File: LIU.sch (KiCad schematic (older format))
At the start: 96 parts, among them J1 Audio Input, J2 Audio Input, J3 12 Volts Input, J4 Audio Output, J5 Audio Output, U1 PT2399, U2 PT2399, U3 L7805, U4 M5226P, U5 M5226P

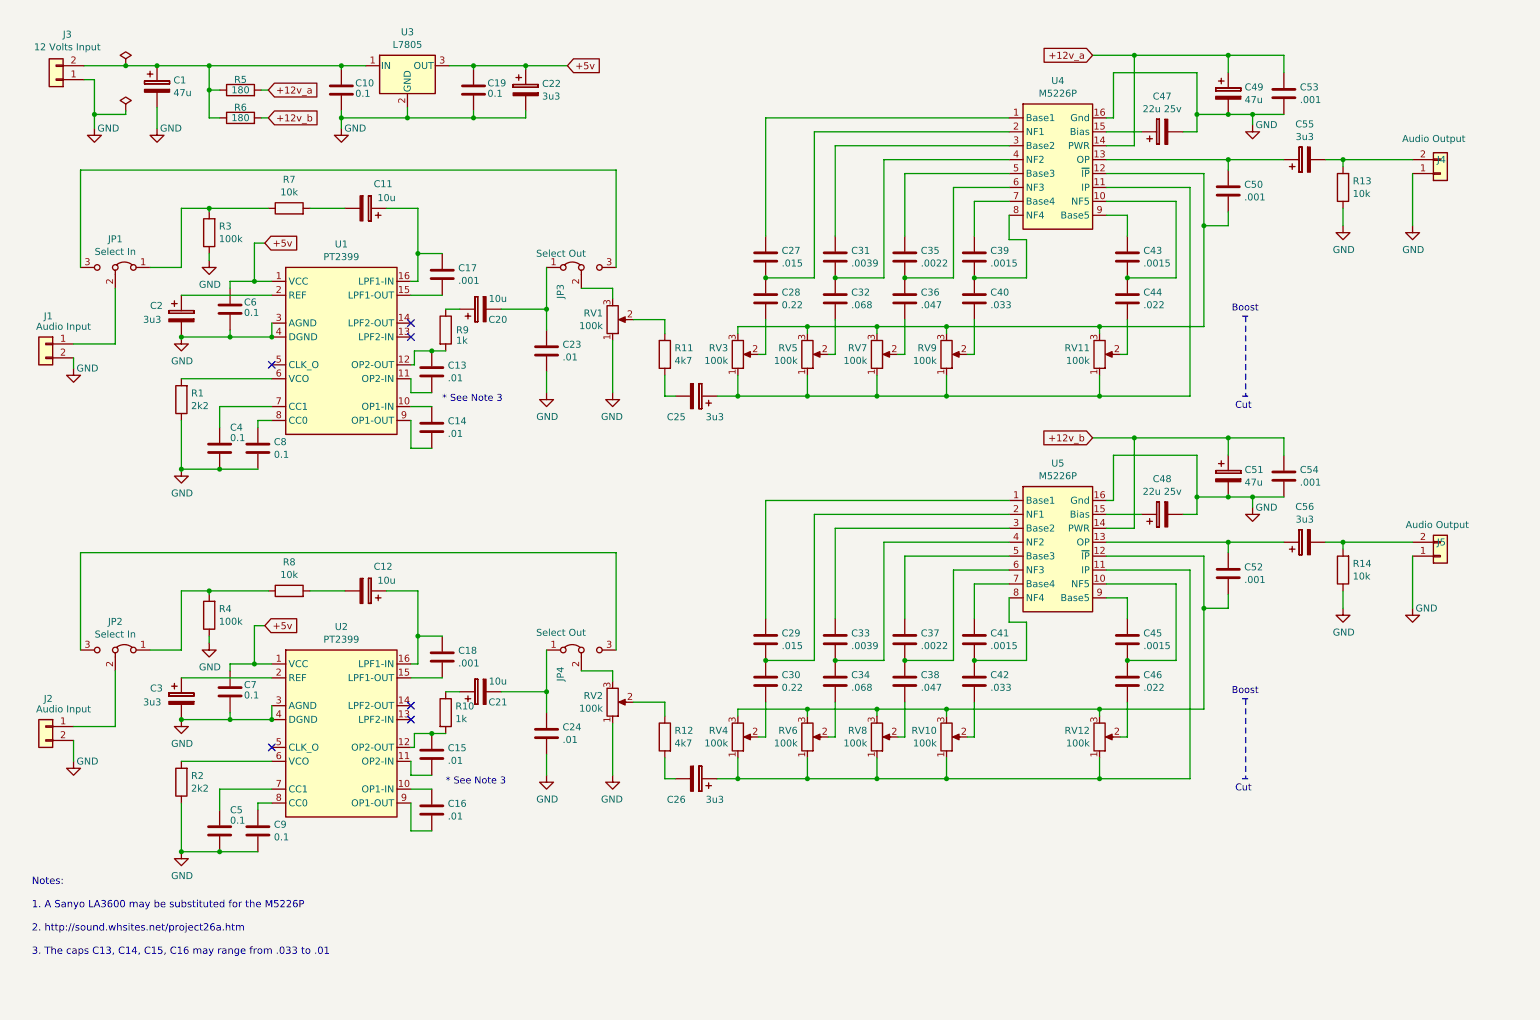
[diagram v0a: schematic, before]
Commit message: Created space in schematic for signaling wiring
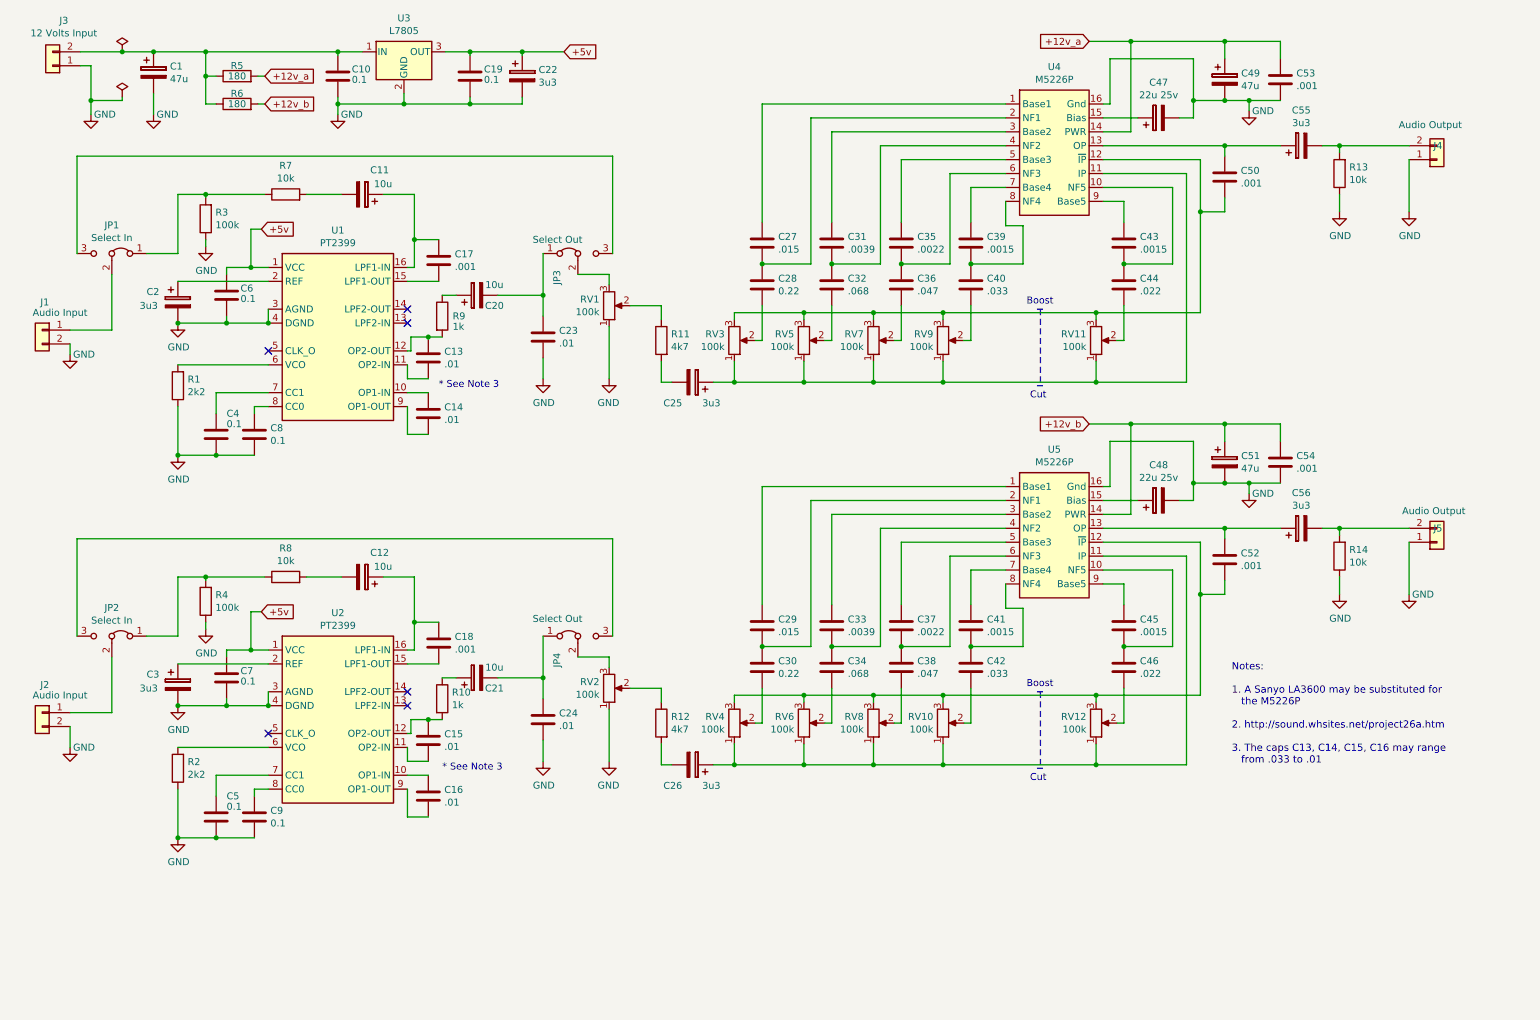
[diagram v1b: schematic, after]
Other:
- note added: "Notes:\n\n1. A Sanyo LA3600 may be substituted for\n the M5226P\n\n2. http://sound.whsites.net/project26a.htm\n\n3. The caps C13, C14, C15, C16 may range\n from .033 to .01\n"
- note removed: "Notes:\n\n1. A Sanyo LA3600 may be substituted for the M5226P\n\n2. http://sound.whsites.net/project26a.htm\n\n3. The caps C13, C14, C15, C16 may range from .033 to .01\n"
- moved on the sheet: C1, C10, C11, C12, C13, C14, C15, C16, C17, C18, C19, C2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

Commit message: Schematic finalised & layout commenced
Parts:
- removed R2: 2k2, symbol Device:R
- added D1, D2: LED_ALT, LED_SMD:LED_1206_3216Metric_Pad1.42x1.75mm_HandSolder, symbol Device:LED_ALT
- added H1, H2, H3, H4: MountingHole, MountingHole:MountingHole_3.2mm_M3, symbol Mechanical:MountingHole
- added J3: UHF out, Connector_PinHeader_2.54mm:PinHeader_1x02_P2.54mm_Vertical, symbol Connector_Generic:Conn_01x02
- added J4: UHF in, Connector_PinHeader_2.54mm:PinHeader_1x02_P2.54mm_Vertical, symbol Connector_Generic:Conn_01x02
- added J6: VHF in, Connector_PinHeader_2.54mm:PinHeader_1x02_P2.54mm_Vertical, symbol Connector_Generic:Conn_01x02
- added J7: VHF out, Connector_PinHeader_2.54mm:PinHeader_1x02_P2.54mm_Vertical, symbol Connector_Generic:Conn_01x02
- added Q1, Q2: 2N7002, Package_TO_SOT_SMD:SOT-23_Handsoldering, symbol Transistor_FET:2N7002
- added R10, R9: 100k, Resistor_SMD:R_1206_3216Metric_Pad1.42x1.75mm_HandSolder, symbol Device:R
- added R13, R14: 10k, Resistor_SMD:R_1206_3216Metric_Pad1.42x1.75mm_HandSolder, symbol Device:R
- added R15, R18, R4: 2k2, Resistor_SMD:R_1206_3216Metric_Pad1.42x1.75mm_HandSolder, symbol Device:R
- added RV1, RV2: 10k, Potentiometer_THT:Potentiometer_Bourns_3386P_Vertical, symbol Device:R_POT
- C1, C49, C51: footprint (none) -> Capacitor_SMD:CP_Elec_6.3x5.2
- C10, C13, C14, C15, C16, C17, C18, C19, C23, C24, C27, C28, C29, C30, C31, C32, C33, C34, C35, C36, C37, C38, C39, C4, C40, C41, C42, C43, C44, C45, C46, C5, C50, C52, C53, C54, C6, C7, C8, C9: footprint (none) -> Capacitor_SMD:C_1206_3216Metric_Pad1.42x1.75mm_HandSolder
- C11, C12, C2, C20, C21, C22, C25, C26, C3, C47, C48, C55, C56: footprint (none) -> Capacitor_SMD:CP_Elec_5x5.3
- J1, J2: footprint (none) -> Connector_PinHeader_2.54mm:PinHeader_1x02_P2.54mm_Vertical
- J5: renamed from J3; footprint (none) -> Connector_PinHeader_2.54mm:PinHeader_1x02_P2.54mm_Vertical
- J8: renamed from J4; footprint (none) -> Connector_PinHeader_2.54mm:PinHeader_1x02_P2.54mm_Vertical
- J9: renamed from J5; footprint (none) -> Connector_PinHeader_2.54mm:PinHeader_1x02_P2.54mm_Vertical
- JP1, JP2, JP3, JP4: footprint (none) -> Connector_PinHeader_2.54mm:PinHeader_1x03_P2.54mm_Vertical
- R1: renamed from R3; footprint (none) -> Resistor_SMD:R_1206_3216Metric_Pad1.42x1.75mm_HandSolder
- R11: renamed from R9; footprint (none) -> Resistor_SMD:R_1206_3216Metric_Pad1.42x1.75mm_HandSolder
- R12: renamed from R10; footprint (none) -> Resistor_SMD:R_1206_3216Metric_Pad1.42x1.75mm_HandSolder
- R16: renamed from R11; footprint (none) -> Resistor_SMD:R_1206_3216Metric_Pad1.42x1.75mm_HandSolder
- R17: renamed from R12; footprint (none) -> Resistor_SMD:R_1206_3216Metric_Pad1.42x1.75mm_HandSolder
- R19: renamed from R13; footprint (none) -> Resistor_SMD:R_1206_3216Metric_Pad1.42x1.75mm_HandSolder
- R2: renamed from R4; footprint (none) -> Resistor_SMD:R_1206_3216Metric_Pad1.42x1.75mm_HandSolder
- R20: renamed from R14; footprint (none) -> Resistor_SMD:R_1206_3216Metric_Pad1.42x1.75mm_HandSolder
- R3: renamed from R1; footprint (none) -> Resistor_SMD:R_1206_3216Metric_Pad1.42x1.75mm_HandSolder
- R5, R6, R7, R8: footprint (none) -> Resistor_SMD:R_1206_3216Metric_Pad1.42x1.75mm_HandSolder
- RV10: renamed from RV8; footprint (none) -> Potentiometer_THT:Potentiometer_Bourns_3386P_Vertical
- RV11: renamed from RV9; footprint (none) -> Potentiometer_THT:Potentiometer_Bourns_3386P_Vertical
- RV12: renamed from RV10; footprint (none) -> Potentiometer_THT:Potentiometer_Bourns_3386P_Vertical
- RV13: renamed from RV11; footprint (none) -> Potentiometer_THT:Potentiometer_Bourns_3386P_Vertical
- RV14: renamed from RV12; footprint (none) -> Potentiometer_THT:Potentiometer_Bourns_3386P_Vertical
- RV3: renamed from RV1; value 100k -> 10k; footprint (none) -> Potentiometer_THT:Potentiometer_Bourns_3386P_Vertical
- RV4: renamed from RV2; value 100k -> 10k; footprint (none) -> Potentiometer_THT:Potentiometer_Bourns_3386P_Vertical
- RV5: renamed from RV3; footprint (none) -> Potentiometer_THT:Potentiometer_Bourns_3386P_Vertical
- RV6: renamed from RV4; footprint (none) -> Potentiometer_THT:Potentiometer_Bourns_3386P_Vertical
- RV7: renamed from RV5; footprint (none) -> Potentiometer_THT:Potentiometer_Bourns_3386P_Vertical
- RV8: renamed from RV6; footprint (none) -> Potentiometer_THT:Potentiometer_Bourns_3386P_Vertical
- RV9: renamed from RV7; footprint (none) -> Potentiometer_THT:Potentiometer_Bourns_3386P_Vertical
- U1, U2: footprint (none) -> Package_DIP:DIP-16_W7.62mm_LongPads
- U3: footprint (none) -> Package_TO_SOT_THT:TO-220-3_Horizontal_TabDown
- U4, U5: footprint (none) -> Package_DIP:DIP-16_W7.62mm_LongPads; symbol Audio_gj:M5226P -> LIU-rescue:M5226P-Audio_gj
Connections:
- wire segments 327 -> 387
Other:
- note added: "Mounting holes are on 92mm centres."
- moved on the sheet: C12, C15, C16, C17, C18, C21, C24, C26, C29, C3, C30, C33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

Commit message: Updated libraries to latest version
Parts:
- U4, U5: symbol LIU-rescue:M5226P-Audio_gj -> LIU-rescue:M5226P-Audio_gj-LIU-rescue
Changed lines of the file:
@@
 $EndDescr
 $Comp
-L LIU-rescue:M5226P-Audio_gj U4
+L LIU-rescue:M5226P-Audio_gj-LIU-rescue U4
 U 1 1 5BB2C5EE
 P 8025 1500
@@
 	5250 3200 5325 3200
 $Comp
-L LIU-rescue:M5226P-Audio_gj U5
+L LIU-rescue:M5226P-Audio_gj-LIU-rescue U5
 U 1 1 5BFD85DB
 P 8025 4125

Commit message: Further layout work
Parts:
- U4, U5: symbol LIU-rescue:M5226P-Audio_gj-LIU-rescue -> LIU-rescue:M5226P-Audio_gj-LIU-rescue-LIU-rescue
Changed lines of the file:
@@
 $EndDescr
 $Comp
-L LIU-rescue:M5226P-Audio_gj-LIU-rescue U4
+L LIU-rescue:M5226P-Audio_gj-LIU-rescue-LIU-rescue U4
 U 1 1 5BB2C5EE
 P 8025 1500
@@
 	5250 3200 5325 3200
 $Comp
-L LIU-rescue:M5226P-Audio_gj-LIU-rescue U5
+L LIU-rescue:M5226P-Audio_gj-LIU-rescue-LIU-rescue U5
 U 1 1 5BFD85DB
 P 8025 4125

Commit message: All components on the board
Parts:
- J1, J2: value Audio Input -> Audio In
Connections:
- net GND: now also J1.1 (Pin_1), J2.1 (Pin_1), J3.1 (Pin_1), J4.1 (Pin_1), J6.1 (Pin_1), J7.1 (Pin_1); no longer J1.2 (Pin_2), J2.2 (Pin_2), J3.2 (Pin_2), J4.2 (Pin_2), J6.2 (Pin_2), J7.2 (Pin_2)
- net at JP1.2 (C): now also J1.2 (Pin_2); no longer J1.1 (Pin_1)
- net at JP2.2 (C): now also J2.2 (Pin_2); no longer J2.1 (Pin_1)
- net at Q2.1 (G), R9.2: now also J3.2 (Pin_2), J6.2 (Pin_2); no longer J3.1 (Pin_1), J6.1 (Pin_1)
- net at Q1.1 (G), R10.2: now also J4.2 (Pin_2), J7.2 (Pin_2); no longer J4.1 (Pin_1), J7.1 (Pin_1)
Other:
- moved on the sheet: J4, J7
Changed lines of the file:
@@
 L Connector_Generic:Conn_01x02 J1
 U 1 1 5BB3D09E
-P 800 2825
-F 0 "J1" H 750 3025 50  0000 L CNN
-F 1 "Audio Input" H 475 2950 50  0000 L CNN
-F 2 "Connector_PinHeader_2.54mm:PinHeader_1x02_P2.54mm_Vertical" H 800 2825 50  0001 C CNN
-F 3 "~" H 800 2825 50  0001 C CNN
-	1    800  2825
-	-1   0    0    -1
+P 800 2925
+F 0 "J1" H 750 3050 50  0000 L CNN
+F 1 "Audio In" H 600 2675 50  0000 L CNN
+F 2 "Connector_PinHeader_2.54mm:PinHeader_1x02_P2.54mm_Vertical" H 800 2925 50  0001 C CNN
+F 3 "~" H 800 2925 50  0001 C CNN
+	1    800  2925
+	-1   0    0    1
 $EndComp
 Wire Wire Line
@@
 L Connector_Generic:Conn_01x02 J2
 U 1 1 5BFD86A7
-P 800 5325
-F 0 "J2" H 750 5525 50  0000 L CNN
-F 1 "Audio Input" H 475 5450 50  0000 L CNN
-F 2 "Connector_PinHeader_2.54mm:PinHeader_1x02_P2.54mm_Vertical" H 800 5325 50  0001 C CNN
-F 3 "~" H 800 5325 50  0001 C CNN
-	1    800  5325
-	-1   0    0    -1
+P 800 5425
+F 0 "J2" H 775 5575 50  0000 L CNN
+F 1 "Audio In" H 600 5175 50  0000 L CNN
+F 2 "Connector_PinHeader_2.54mm:PinHeader_1x02_P2.54mm_Vertical" H 800 5425 50  0001 C CNN
+F 3 "~" H 800 5425 50  0001 C CNN
+	1    800  5425
+	-1   0    0    1
 $EndComp
 Wire Wire Line
@@
 P 1000 3000
 F 0 "#PWR01" H 1000 2750 50  0001 C CNN
-F 1 "GND" H 1100 3000 50  0000 C CNN
+F 1 "GND" H 1100 3000 50  0001 C CNN
 F 2 "" H 1000 3000 50  0001 C CNN
 F 3 "" H 1000 3000 50  0001 C CNN
@@
 P 1000 5575
 F 0 "#PWR02" H 1000 5325 50  0001 C CNN
-F 1 "GND" H 1100 5575 50  0000 C CNN
+F 1 "GND" H 1100 5575 50  0001 C CNN
 F 2 "" H 1000 5575 50  0001 C CNN
 F 3 "" H 1000 5575 50  0001 C CNN
@@
 L Connector_Generic:Conn_01x02 J3
 U 1 1 5C0E0F4F
-P 800 6775
-F 0 "J3" H 750 6975 50  0000 L CNN
-F 1 "UHF out" H 475 6900 50  0000 L CNN
-F 2 "Connector_PinHeader_2.54mm:PinHeader_1x02_P2.54mm_Vertical" H 800 6775 50  0001 C CNN
-F 3 "~" H 800 6775 50  0001 C CNN
-	1    800  6775
-	-1   0    0    -1
+P 800 6875
+F 0 "J3" H 750 7000 50  0000 L CNN
+F 1 "UHF out" H 625 6650 50  0000 L CNN
+F 2 "Connector_PinHeader_2.54mm:PinHeader_1x02_P2.54mm_Vertical" H 800 6875 50  0001 C CNN
+F 3 "~" H 800 6875 50  0001 C CNN
+	1    800  6875
+	-1   0    0    1
 $EndComp
 $Comp
 L Connector_Generic:Conn_01x02 J4
 U 1 1 5C0E11B5
-P 825 7425
-F 0 "J4" H 775 7625 50  0000 L CNN
-F 1 "UHF in" H 500 7550 50  0000 L CNN
-F 2 "Connector_PinHeader_2.54mm:PinHeader_1x02_P2.54mm_Vertical" H 825 7425 50  0001 C CNN
-F 3 "~" H 825 7425 50  0001 C CNN
-	1    825  7425
-	-1   0    0    -1
+P 800 7525
+F 0 "J4" H 750 7650 50  0000 L CNN
+F 1 "UHF in" H 675 7300 50  0000 L CNN
+F 2 "Connector_PinHeader_2.54mm:PinHeader_1x02_P2.54mm_Vertical" H 800 7525 50  0001 C CNN
+F 3 "~" H 800 7525 50  0001 C CNN
+	1    800  7525
+	-1   0    0    1
 $EndComp
 $Comp
 L Connector_Generic:Conn_01x02 J6
 U 1 1 5C0E1666
-P 2850 6775
-F 0 "J6" H 2825 6550 50  0000 L CNN
-F 1 "VHF in" H 2950 6725 50  0000 L CNN
-F 2 "Connector_PinHeader_2.54mm:PinHeader_1x02_P2.54mm_Vertical" H 2850 6775 50  0001 C CNN
-F 3 "~" H 2850 6775 50  0001 C CNN
-	1    2850 6775
-	1    0    0    -1
+P 2850 6875
+F 0 "J6" H 2825 7000 50  0000 L CNN
+F 1 "VHF in" H 2775 6675 50  0000 L CNN
+F 2 "Connector_PinHeader_2.54mm:PinHeader_1x02_P2.54mm_Vertical" H 2850 6875 50  0001 C CNN
+F 3 "~" H 2850 6875 50  0001 C CNN
+	1    2850 6875
+	1    0    0    1
 $EndComp
 $Comp
 L Connector_Generic:Conn_01x02 J7
 U 1 1 5C0E166D
-P 2875 7425
-F 0 "J7" H 2825 7200 50  0000 L CNN
-F 1 "VHF out" H 2950 7375 50  0000 L CNN
-F 2 "Connector_PinHeader_2.54mm:PinHeader_1x02_P2.54mm_Vertical" H 2875 7425 50  0001 C CNN
-F 3 "~" H 2875 7425 50  0001 C CNN
-	1    2875 7425
-	1    0    0    -1
+P 2850 7525
+F 0 "J7" H 2825 7650 50  0000 L CNN
+F 1 "VHF out" H 2775 7300 50  0000 L CNN
+F 2 "Connector_PinHeader_2.54mm:PinHeader_1x02_P2.54mm_Vertical" H 2850 7525 50  0001 C CNN
+F 3 "~" H 2850 7525 50  0001 C CNN
+	1    2850 7525
+	1    0    0    1
 $EndComp
 $Comp
@@
 L power:GND #PWR04
 U 1 1 5C14CDB7
-P 1025 7575
-F 0 "#PWR04" H 1025 7325 50  0001 C CNN
-F 1 "GND" H 1125 7575 50  0001 C CNN
-F 2 "" H 1025 7575 50  0001 C CNN
-F 3 "" H 1025 7575 50  0001 C CNN
-	1    1025 7575
-	1    0    0    -1
-$EndComp
-Wire Wire Line
-	1025 7525 1025 7575
+P 1000 7575
+F 0 "#PWR04" H 1000 7325 50  0001 C CNN
+F 1 "GND" H 1100 7575 50  0001 C CNN
+F 2 "" H 1000 7575 50  0001 C CNN
+F 3 "" H 1000 7575 50  0001 C CNN
+	1    1000 7575
+	1    0    0    -1
+$EndComp
+Wire Wire Line
+	1000 7525 1000 7575
 $Comp
 L power:GND #PWR013
@@
 L power:GND #PWR014
 U 1 1 5C171DCD
-P 2675 7575
-F 0 "#PWR014" H 2675 7325 50  0001 C CNN
-F 1 "GND" H 2775 7575 50  0001 C CNN
-F 2 "" H 2675 7575 50  0001 C CNN
-F 3 "" H 2675 7575 50  0001 C CNN
-	1    2675 7575
-	1    0    0    -1
-$EndComp
-Wire Wire Line
-	2675 7525 2675 7575
+P 2650 7575
+F 0 "#PWR014" H 2650 7325 50  0001 C CNN
+F 1 "GND" H 2750 7575 50  0001 C CNN
+F 2 "" H 2650 7575 50  0001 C CNN
+F 3 "" H 2650 7575 50  0001 C CNN
+	1    2650 7575
+	1    0    0    -1
+$EndComp
+Wire Wire Line
+	2650 7525 2650 7575
 Wire Wire Line
 	2650 6875 2650 6925
@@
 $EndComp
 Wire Wire Line
-	1025 7425 2575 7425
+	1000 7425 2575 7425
 Wire Wire Line
 	2575 7425 2575 7200
@@
 Connection ~ 2575 7425
 Wire Wire Line
-	2575 7425 2675 7425
+	2575 7425 2650 7425
 Wire Wire Line
 	2575 6775 2575 6625
@@
 	4050 7375 4050 7575
 $Comp
-L power:GND #PWR?
+L power:GND #PWR0101
 U 1 1 5C19559C
 P 5100 7575
-F 0 "#PWR?" H 5100 7325 50  0001 C CNN
+F 0 "#PWR0101" H 5100 7325 50  0001 C CNN
 F 1 "GND" H 5105 7402 50  0001 C CNN
 F 2 "" H 5100 7575 50  0001 C CNN
@@
 	5100 7375 5100 7575
 $Comp
-L power:GND #PWR?
+L power:GND #PWR0102
 U 1 1 5C1BDE3A
 P 4625 7575
-F 0 "#PWR?" H 4625 7325 50  0001 C CNN
+F 0 "#PWR0102" H 4625 7325 50  0001 C CNN
 F 1 "GND" H 4630 7402 50  0001 C CNN
 F 2 "" H 4625 7575 50  0001 C CNN

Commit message: Synchronised libraries on both machines
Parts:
- U4, U5: symbol LIU-rescue:M5226P-Audio_gj-LIU-rescue-LIU-rescue -> LIU-rescue:M5226P-Audio_gj-LIU-rescue-LIU-rescue-LIU-rescue
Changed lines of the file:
@@
 $EndDescr
 $Comp
-L LIU-rescue:M5226P-Audio_gj-LIU-rescue-LIU-rescue U4
+L LIU-rescue:M5226P-Audio_gj-LIU-rescue-LIU-rescue-LIU-rescue U4
 U 1 1 5BB2C5EE
 P 8025 1500
@@
 	5250 3200 5325 3200
 $Comp
-L LIU-rescue:M5226P-Audio_gj-LIU-rescue-LIU-rescue U5
+L LIU-rescue:M5226P-Audio_gj-LIU-rescue-LIU-rescue-LIU-rescue U5
 U 1 1 5BFD85DB
 P 8025 4125

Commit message: Further PCB layout
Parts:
- removed U4, U5: M5226P, Package_DIP:DIP-16_W7.62mm_LongPads, symbol LIU-rescue:M5226P-Audio_gj-LIU-rescue-LIU-rescue-LIU-rescue
- added U4, U5: M5226P, Package_DIP:DIP-16_W7.62mm_LongPads, symbol Audio_gj:M5226P
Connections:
- net +12v_a: now also U4.14 (PWR)
- net +12v_b: now also U5.14 (PWR)
- net GND: now also U4.16 (Gnd), U5.16 (Gnd)
- net at C27.1: now also U4.1 (Base1)
- net at C43.2, C44.1: now also U4.10 (NF5)
- net at C25.1, RV11.1, RV13.1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: now also U4.11 (IP)
- net at C50.2, RV11.3, RV13.3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: now also U4.12 (~IP)
- net at C50.1, C55.1: now also U4.13 (OP)
- net at C47.1: now also U4.15 (Bias)
- net at C27.2, C28.1: now also U4.2 (NF1)
- net at C31.1: now also U4.3 (Base2)
- net at C31.2, C32.1: now also U4.4 (NF2)
- net at C35.1: now also U4.5 (Base3)
- net at C35.2, C36.1: now also U4.6 (NF3)
- net at C39.1: now also U4.7 (Base4)
- net at C39.2, C40.1: now also U4.8 (NF4)
- net at C43.1: now also U4.9 (Base5)
- net at C29.1: now also U5.1 (Base1)
- net at C45.2, C46.1: now also U5.10 (NF5)
- net at C26.1, RV10.1, RV12.1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: now also U5.11 (IP)
- net at C52.2, RV10.3, RV12.3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: now also U5.12 (~IP)
- net at C52.1, C56.1: now also U5.13 (OP)
- net at C48.1: now also U5.15 (Bias)
- net at C29.2, C30.1: now also U5.2 (NF1)
- net at C33.1: now also U5.3 (Base2)
- net at C33.2, C34.1: now also U5.4 (NF2)
- net at C37.1: now also U5.5 (Base3)
- net at C37.2, C38.1: now also U5.6 (NF3)
- net at C41.1: now also U5.7 (Base4)
- net at C41.2, C42.1: now also U5.8 (NF4)
- net at C45.1: now also U5.9 (Base5)
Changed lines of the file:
@@
 $EndDescr
-$Comp
-L LIU-rescue:M5226P-Audio_gj-LIU-rescue-LIU-rescue-LIU-rescue U4
-U 1 1 5BB2C5EE
-P 8025 1500
-F 0 "U4" H 8075 2067 50  0000 C CNN
-F 1 "M5226P" H 8075 1976 50  0000 C CNN
-F 2 "Package_DIP:DIP-16_W7.62mm_LongPads" H 8025 1100 50  0001 C CNN
-F 3 "http://www.elparadise.com/public/epepdfs/M5226P.pdf" H 8025 1100 50  0001 C CNN
-	1    8025 1500
-	1    0    0    -1
-$EndComp
 $Comp
 L Device:R_POT RV9
@@
 	5250 3200 5325 3200
 $Comp
-L LIU-rescue:M5226P-Audio_gj-LIU-rescue-LIU-rescue-LIU-rescue U5
-U 1 1 5BFD85DB
-P 8025 4125
-F 0 "U5" H 8075 4692 50  0000 C CNN
-F 1 "M5226P" H 8075 4601 50  0000 C CNN
-F 2 "Package_DIP:DIP-16_W7.62mm_LongPads" H 8025 3725 50  0001 C CNN
-F 3 "http://www.elparadise.com/public/epepdfs/M5226P.pdf" H 8025 3725 50  0001 C CNN
-	1    8025 4125
-	1    0    0    -1
-$EndComp
-$Comp
 L Device:R_POT RV10
 U 1 1 5BFD85E2
@@
 Wire Wire Line
 	4250 6250 4625 6250
+$Comp
+L Audio_gj:M5226P U4
+U 1 1 5BDF3123
+P 8025 1500
+F 0 "U4" H 8075 2067 50  0000 C CNN
+F 1 "M5226P" H 8075 1976 50  0000 C CNN
+F 2 "Package_DIP:DIP-16_W7.62mm_LongPads" H 8025 1100 50  0001 C CNN
+F 3 "http://www.elparadise.com/public/epepdfs/M5226P.pdf" H 8025 1100 50  0001 C CNN
+	1    8025 1500
+	1    0    0    -1
+$EndComp
+$Comp
+L Audio_gj:M5226P U5
+U 1 1 5BDF3730
+P 8025 4125
+F 0 "U5" H 8075 4692 50  0000 C CNN
+F 1 "M5226P" H 8075 4601 50  0000 C CNN
+F 2 "Package_DIP:DIP-16_W7.62mm_LongPads" H 8025 3725 50  0001 C CNN
+F 3 "http://www.elparadise.com/public/epepdfs/M5226P.pdf" H 8025 3725 50  0001 C CNN
+	1    8025 4125
+	1    0    0    -1
+$EndComp
 $EndSCHEMATC
